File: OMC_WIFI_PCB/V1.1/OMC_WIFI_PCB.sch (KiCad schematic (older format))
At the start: 16 parts, among them J10 Control_ACS712, J11 Control_ZMPT101B, J3 Power_In, J4 Switch, J5 Pins_FT232R, J6 Line_Relay, J7 Control_Relay, J8 Line_ACS712, J9 Line_ZMPT101B, U1 ESP32-WROOM-32

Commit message: PCB v1.1
>Actualización esquemático y PCB
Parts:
- removed J3: Power_In, 6PCV-03-006:TE_5-1437652-4, symbol Connector:Screw_Terminal_01x03
- added J?: Line Input, symbol Connector:Conn_01x01_Male
- added J?: Nuetral Input, symbol Connector:Conn_01x01_Male
- added JP2: OMC-Female-Plug, symbol omc-plugs:OMC-Female-Plug
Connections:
- net NEUTRAL: now also J?.1 (Pin_1)
- net at F1.1, F1.2: now also J?.1 (Pin_1)
- no-connect marks 27 -> 28
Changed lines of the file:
@@
-$EndComp
-$Comp
-L power:PWR_FLAG #FLG0101
-U 1 1 622CF9F0
-P 1250 1200
-F 0 "#FLG0101" H 1250 1275 50  0001 C CNN
-F 1 "PWR_FLAG" H 1250 1373 50  0000 C CNN
-F 2 "" H 1250 1200 50  0001 C CNN
-F 3 "~" H 1250 1200 50  0001 C CNN
-	1    1250 1200
-	1    0    0    -1
 $EndComp
 $Comp
@@
 Text Notes 1000 800  0    50   ~ 10
 Alimentación y Carga
-$Comp
-L Connector:Screw_Terminal_01x03 J3
-U 1 1 6243119F
-P 850 1300
-F 0 "J3" H 768 1617 50  0000 C CNN
-F 1 "Power_In" H 768 1526 50  0000 C CNN
-F 2 "6PCV-03-006:TE_5-1437652-4" H 850 1300 50  0001 C CNN
-F 3 "~" H 850 1300 50  0001 C CNN
-	1    850  1300
-	-1   0    0    -1
-$EndComp
 Wire Wire Line
 	3800 2550 4050 2550
@@
 NoConn ~ 3800 2900
 Wire Wire Line
-	1050 1200 1250 1200
-Wire Wire Line
 	1450 2700 1350 2700
 Wire Wire Line
@@
 Text GLabel 5250 1100 0    50   Input ~ 0
 NO
-Wire Wire Line
-	1400 1200 1250 1200
-Connection ~ 1250 1200
 Wire Notes Line
 	700  1950 2200 1950
@@
 Wire Notes Line
 	2200 600  2200 1950
-Text GLabel 1400 1200 2    50   Input ~ 0
-COM
 Text GLabel 1350 2700 0    50   Input ~ 0
 NEUTRAL
@@
 LINE
 Wire Wire Line
-	1050 1300 1150 1300
-Wire Wire Line
-	1050 1400 1250 1400
-Connection ~ 1250 1400
-Wire Wire Line
 	6750 1250 6900 1250
 Wire Wire Line
@@
 Wire Wire Line
 	1450 1250 1150 1250
-Wire Wire Line
-	1150 1250 1150 1300
-Connection ~ 1150 1300
 Wire Wire Line
 	1900 4250 1750 4250
@@
 Wire Notes Line
 	700  3550 700  7250
+$Comp
+L omc-plugs:OMC-Female-Plug JP2
+U 1 1 6242580B
+P 3500 550
+F 0 "JP2" H 3174 773 50  0000 C CNN
+F 1 "OMC-Female-Plug" H 3174 682 50  0000 C CNN
+F 2 "" H 3492 440 50  0001 C CNN
+F 3 "" H 3492 440 50  0001 C CNN
+	1    3500 550
+	1    0    0    -1
+$EndComp
+NoConn ~ 3426 552
+Wire Wire Line
+	1150 1250 1150 1300
+Wire Wire Line
+	998  1301 1150 1301
+Wire Wire Line
+	1150 1301 1150 1300
+Connection ~ 1150 1300
+$Comp
+L Connector:Conn_01x01_Male J?
+U 1 1 6246AC9C
+P 798 1301
+F 0 "J?" H 906 1482 50  0000 C CNN
+F 1 "Line Input" H 906 1391 50  0000 C CNN
+F 2 "" H 798 1301 50  0001 C CNN
+F 3 "~" H 798 1301 50  0001 C CNN
+	1    798  1301
+	1    0    0    -1
+$EndComp
+$Comp
+L Connector:Conn_01x01_Male J?
+U 1 1 624922FE
+P 907 1401
+F 0 "J?" H 1015 1582 50  0000 C CNN
+F 1 "Nuetral Input" H 957 1357 50  0000 C CNN
+F 2 "" H 907 1401 50  0001 C CNN
+F 3 "~" H 907 1401 50  0001 C CNN
+	1    907  1401
+	1    0    0    -1
+$EndComp
+Wire Wire Line
+	1250 1400 1104 1400
+Wire Wire Line
+	1104 1400 1104 1401
+Wire Wire Line
+	1104 1401 1107 1401
+Connection ~ 1250 1400
 $EndSCHEMATC

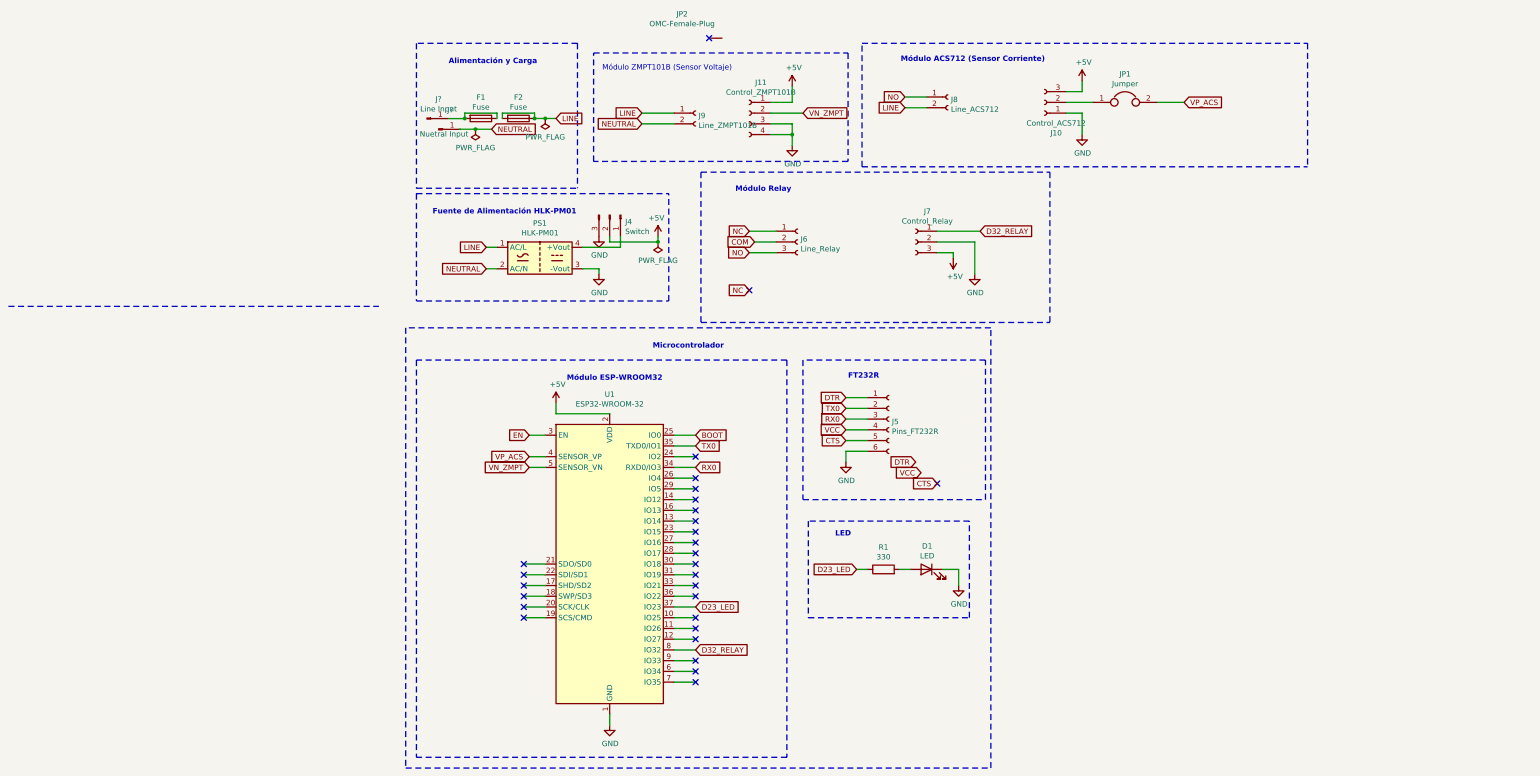
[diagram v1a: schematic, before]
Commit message: Actualización PCB v1.1
+ Alimentación (Input/Output)
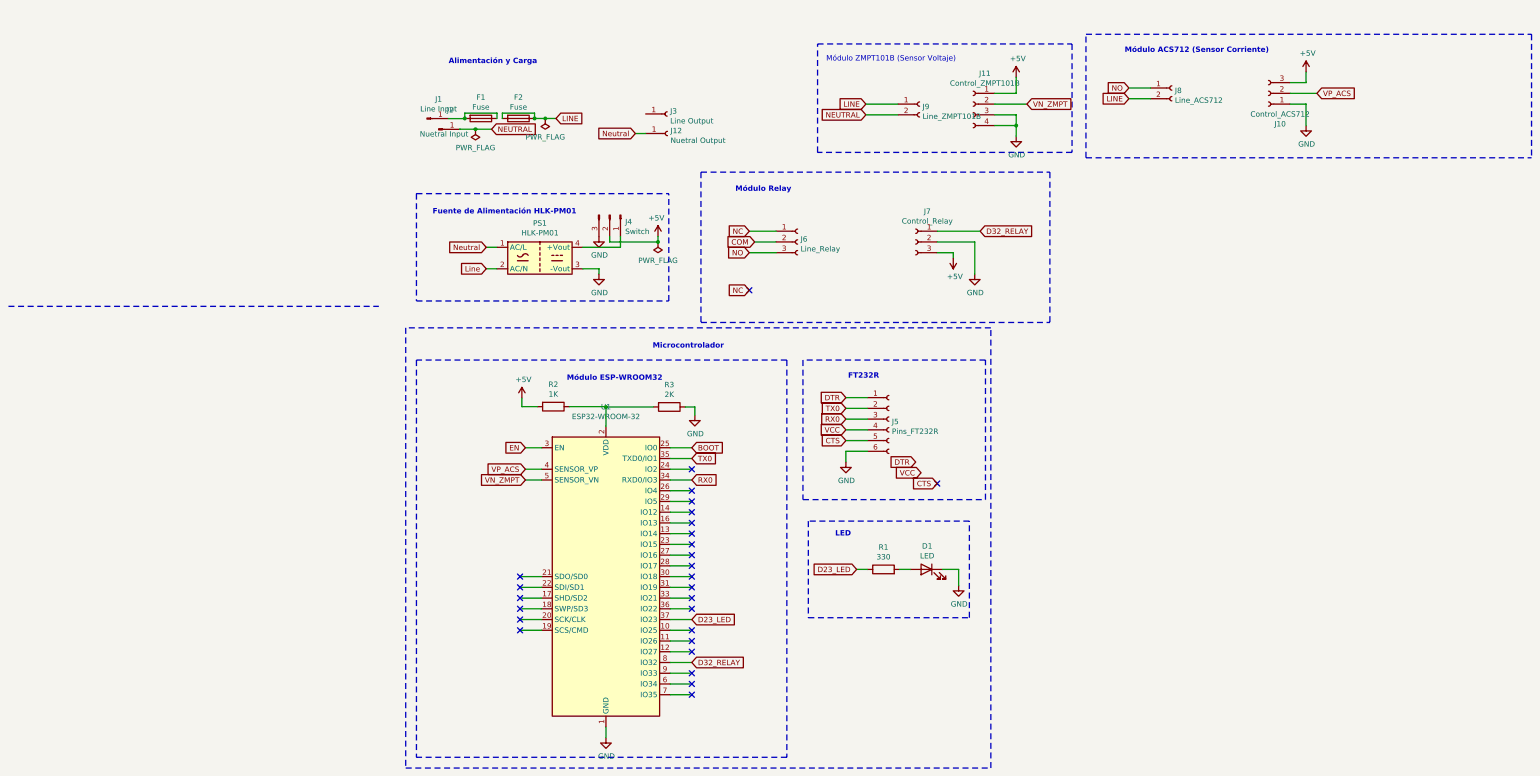
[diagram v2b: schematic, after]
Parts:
- removed JP1: Jumper, Connector_PinHeader_2.54mm:PinHeader_1x02_P2.54mm_Vertical, symbol Device:Jumper
- removed JP2: OMC-Female-Plug, symbol omc-plugs:OMC-Female-Plug
- added J12: Nuetral Output, omc-plugs:OMC-Female-Plug, symbol Connector:Conn_01x01_Female
- added J3: Line Output, omc-plugs:OMC-Female-Plug, symbol Connector:Conn_01x01_Female
- added R2: 1K, Resistor_SMD:R_2512_6332Metric_Pad1.40x3.35mm_HandSolder, symbol Device:R
- added R3: 2K, Resistor_SMD:R_2512_6332Metric_Pad1.40x3.35mm_HandSolder, symbol Device:R
- J1, J2: renamed from J?; footprint (none) -> omc-plugs:OMC-Male-Plug
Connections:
- net +5V: now also R2.2; no longer U1.2 (VDD)
- net GND: now also R3.1
- net LINE: no longer PS1.1 (AC/L)
- net NEUTRAL: no longer PS1.2 (AC/N)
- net VP_ACS: now also J10.2 (Pin_2)
- new net: R2.1, R3.2, U1.2 (VDD)
- new net Line: PS1.2 (AC/N)
- new net Neutral: J12.1 (Pin_1), PS1.1 (AC/L)
- no-connect marks 28 -> 27
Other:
- moved on the sheet: J10, J11, J8, J9, U1

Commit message: Actualización AutoConnect
+ Modificación Labels en página principal
+ Modificación de ítems que aparecen en la página principal
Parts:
- removed R2: 1K, Resistor_SMD:R_2512_6332Metric_Pad1.40x3.35mm_HandSolder, symbol Device:R
- removed R3: 2K, Resistor_SMD:R_2512_6332Metric_Pad1.40x3.35mm_HandSolder, symbol Device:R
- added J?: Conn_01x03_Female, symbol Connector:Conn_01x03_Female
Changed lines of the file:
@@
 L power:+5V #PWR0101
 U 1 1 621F2808
-P 1682 3905
-F 0 "#PWR0101" H 1682 3755 50  0001 C CNN
-F 1 "+5V" H 1697 4078 50  0000 C CNN
-F 2 "" H 1682 3905 50  0001 C CNN
-F 3 "" H 1682 3905 50  0001 C CNN
-	1    1682 3905
+P 1110 3783
+F 0 "#PWR0101" H 1110 3633 50  0001 C CNN
+F 1 "+5V" H 1125 3956 50  0000 C CNN
+F 2 "" H 1110 3783 50  0001 C CNN
+F 3 "" H 1110 3783 50  0001 C CNN
+	1    1110 3783
 	1    0    0    -1
 $EndComp
@@
 	1104 1401 1107 1401
 Connection ~ 1250 1400
-$Comp
-L Device:R R3
-U 1 1 62488DE2
-P 3055 3987
-F 0 "R3" V 2848 3987 50  0000 C CNN
-F 1 "2K" V 2939 3987 50  0000 C CNN
-F 2 "Resistor_SMD:R_2512_6332Metric_Pad1.40x3.35mm_HandSolder" V 2985 3987 50  0001 C CNN
-F 3 "~" H 3055 3987 50  0001 C CNN
-	1    3055 3987
-	0    1    1    0
-$EndComp
 $Comp
 L RF_Module:ESP32-WROOM-32 U1
@@
 Text GLabel 1715 4367 0    50   Input ~ 0
 EN
-$Comp
-L Device:R R2
-U 1 1 6247BBA5
-P 1975 3984
-F 0 "R2" V 1768 3984 50  0000 C CNN
-F 1 "1K" V 1859 3984 50  0000 C CNN
-F 2 "Resistor_SMD:R_2512_6332Metric_Pad1.40x3.35mm_HandSolder" V 1905 3984 50  0001 C CNN
-F 3 "~" H 1975 3984 50  0001 C CNN
-	1    1975 3984
-	0    1    1    0
-$EndComp
-Wire Wire Line
-	2465 3987 2905 3987
-Wire Wire Line
-	2125 3984 2465 3984
-Wire Wire Line
-	2465 3984 2465 3987
-Connection ~ 2465 3987
-Wire Wire Line
-	2465 3987 2465 4167
 Wire Wire Line
 	1825 3984 1682 3984
@@
 $EndComp
 Wire Wire Line
-	3205 3987 3293 3987
-Wire Wire Line
-	3293 3987 3293 4064
-Wire Wire Line
 	9087 1066 8836 1066
 $Comp
@@
 Wire Wire Line
 	2838 1440 2739 1440
+$Comp
+L Connector:Conn_01x03_Female J?
+U 1 1 624BB1DC
+P 1530 3938
+F 0 "J?" H 1558 3964 50  0000 L CNN
+F 1 "Conn_01x03_Female" H 1558 3873 50  0000 L CNN
+F 2 "" H 1530 3938 50  0001 C CNN
+F 3 "~" H 1530 3938 50  0001 C CNN
+	1    1530 3938
+	1    0    0    -1
+$EndComp
 $EndSCHEMATC
